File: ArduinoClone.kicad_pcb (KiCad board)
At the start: 2 copper layers, 0 parts

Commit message: added design rules
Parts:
- added BT1: Battery 3V, Connector_PinHeader_2.54mm:PinHeader_1x02_P2.54mm_Vertical, F.Cu at (177.0, 88.4)
- added C1: 22pF, Capacitor_SMD:C_0805_2012Metric_Pad1.15x1.40mm_HandSolder, F.Cu at (181.7, 87.6)
- added C2: 22pF, Capacitor_SMD:C_0805_2012Metric_Pad1.15x1.40mm_HandSolder, F.Cu at (177.0, 94.8)
- added C3: 10uF, Capacitor_SMD:C_0805_2012Metric_Pad1.15x1.40mm_HandSolder, F.Cu at (181.7, 90.5)
- added D1: LED, LED_SMD:LED_0805_2012Metric_Pad1.15x1.40mm_HandSolder, F.Cu at (170.8, 96.7)
- added J1: Serial, Connector_PinSocket_2.54mm:PinSocket_1x04_P2.54mm_Vertical, F.Cu at (94.4, 77.2)
- added J2: Digital pins, Connector_PinSocket_2.54mm:PinSocket_1x09_P2.54mm_Vertical, F.Cu at (89.8, 77.2)
- added J3: I2C, Connector_PinSocket_2.54mm:PinSocket_1x04_P2.54mm_Vertical, F.Cu at (99.0, 77.2)
- added J4: ICSP, Connector_PinSocket_2.54mm:PinSocket_2x03_P2.54mm_Vertical, F.Cu at (106.2, 77.2)
- added R1: 330R, Resistor_SMD:R_0805_2012Metric_Pad1.15x1.40mm_HandSolder, F.Cu at (175.6, 97.7)
- added R2: 10K, Resistor_SMD:R_0805_2012Metric_Pad1.15x1.40mm_HandSolder, F.Cu at (181.8, 93.5)
- added U1: DS1337S+, Package_SO:SO-8_5.3x6.2mm_P1.27mm, F.Cu at (158.0, 96.6)
- added U2: 24LC1025, Package_SO:SOIJ-8_5.3x5.3mm_P1.27mm, F.Cu at (169.4, 84.7)
- added U3: 24LC1025, Package_SO:SOIJ-8_5.3x5.3mm_P1.27mm, F.Cu at (169.4, 91.7)
- added U4: ATMEGA328-AU, digikey-footprints:TQFP-32_7x7mm, F.Cu at (158.4, 87.0)
- added Y1: Crystal 32MHz, Crystal:Crystal_SMD_MicroCrystal_CC7V-T1A-2Pin_3.2x1.5mm, F.Cu at (165.9, 96.9)
- added Y2: Crystal 16MHz, Crystal:Crystal_SMD_5032-2Pin_5.0x3.2mm_HandSoldering, F.Cu at (179.8, 83.7)
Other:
- net class Power added: clearance 0.2, trace_width 0.3, via_dia 1, via_drill 0.6

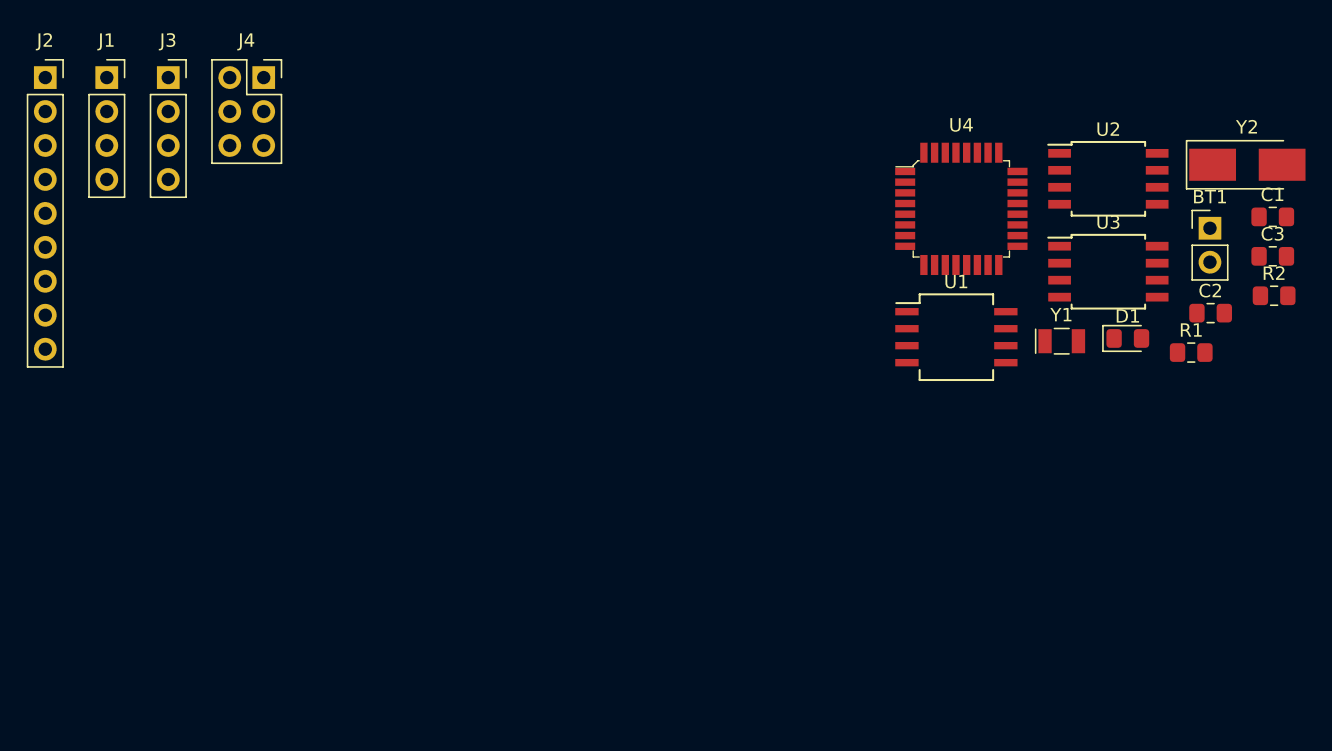
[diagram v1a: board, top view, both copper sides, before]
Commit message: corrected error inschematic and placed components in pcbnew
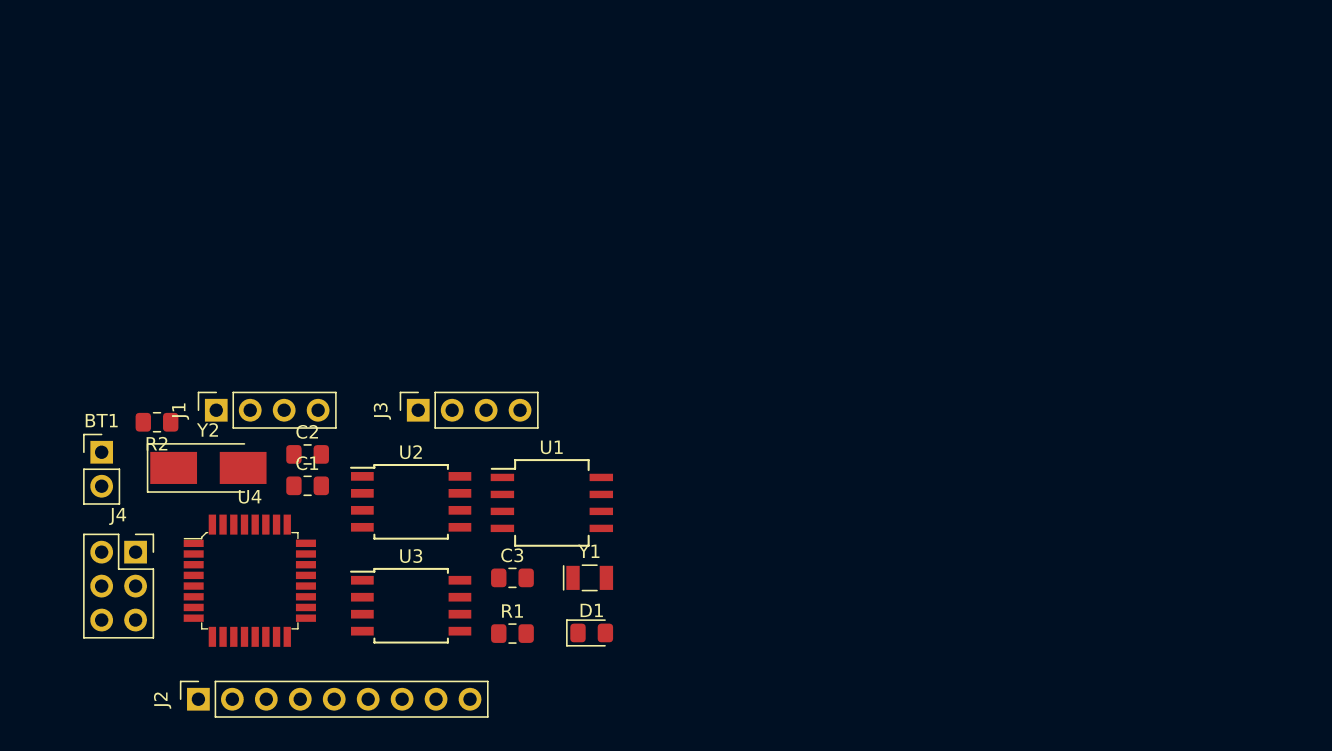
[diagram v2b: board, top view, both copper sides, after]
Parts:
- moved BT1 84.6 mm to (94.1, 105.2)
- moved R2 84.1 mm to (98.2, 102.9), turned to 180 degrees
- moved Y2 81.0 mm to (102.0, 106.4)
- moved C1 75.0 mm to (109.5, 107.7)
- moved C2 68.4 mm to (109.5, 105.3)
- moved C3 61.8 mm to (124.8, 114.6)
- moved U4 60.1 mm to (105.1, 114.8)
- moved U3 57.8 mm to (117.2, 116.7)
- moved U2 57.5 mm to (117.2, 108.9)
- moved R1 55.0 mm to (124.8, 118.7)
- moved J2 47.9 mm to (101.3, 123.7), turned to 90 degrees
- moved D1 45.8 mm to (130.7, 118.7)
- moved Y1 39.5 mm to (130.6, 114.6)
- moved J4 36.8 mm to (96.6, 112.7)
- moved U1 32.7 mm to (127.7, 109.0)
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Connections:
- BT1 pad 2: Net-(BT1-Pad2) -> GNDPWR
- C3 pad 1: Net-(BT1-Pad2) -> /Vcc

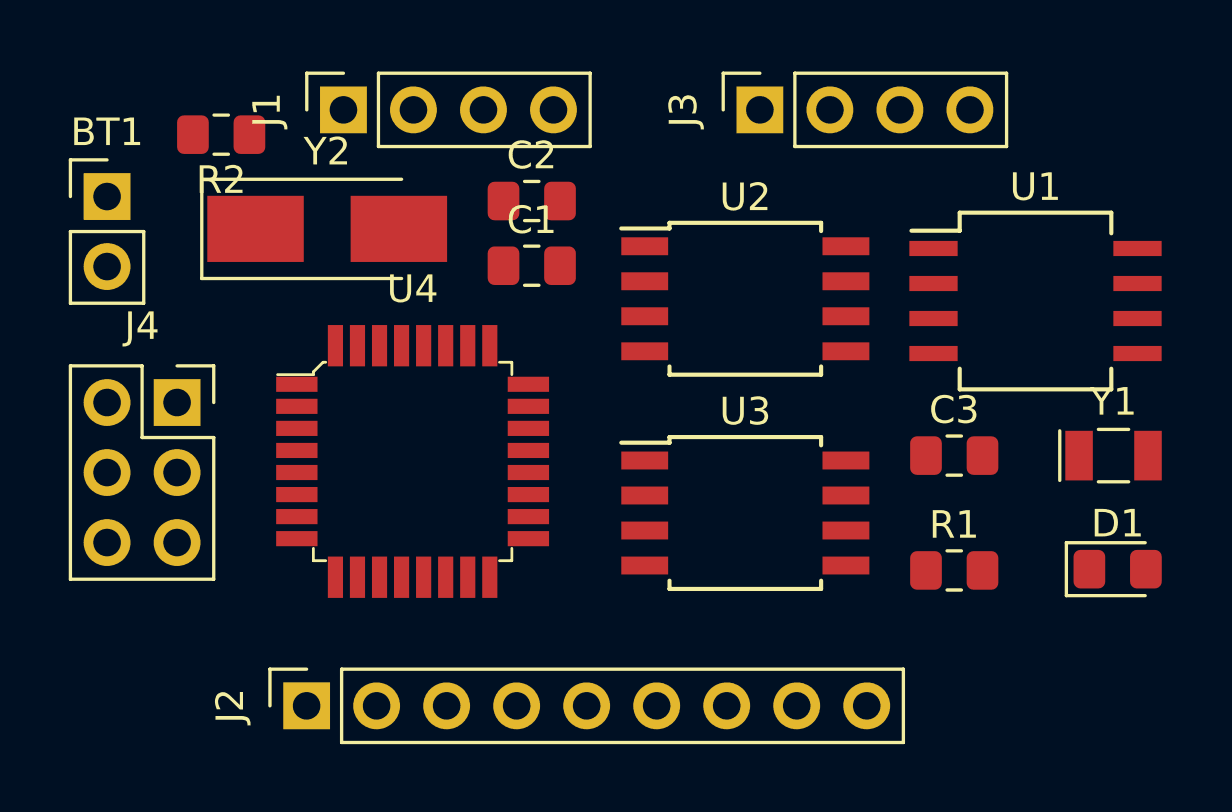
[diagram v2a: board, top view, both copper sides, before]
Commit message: added edges to board
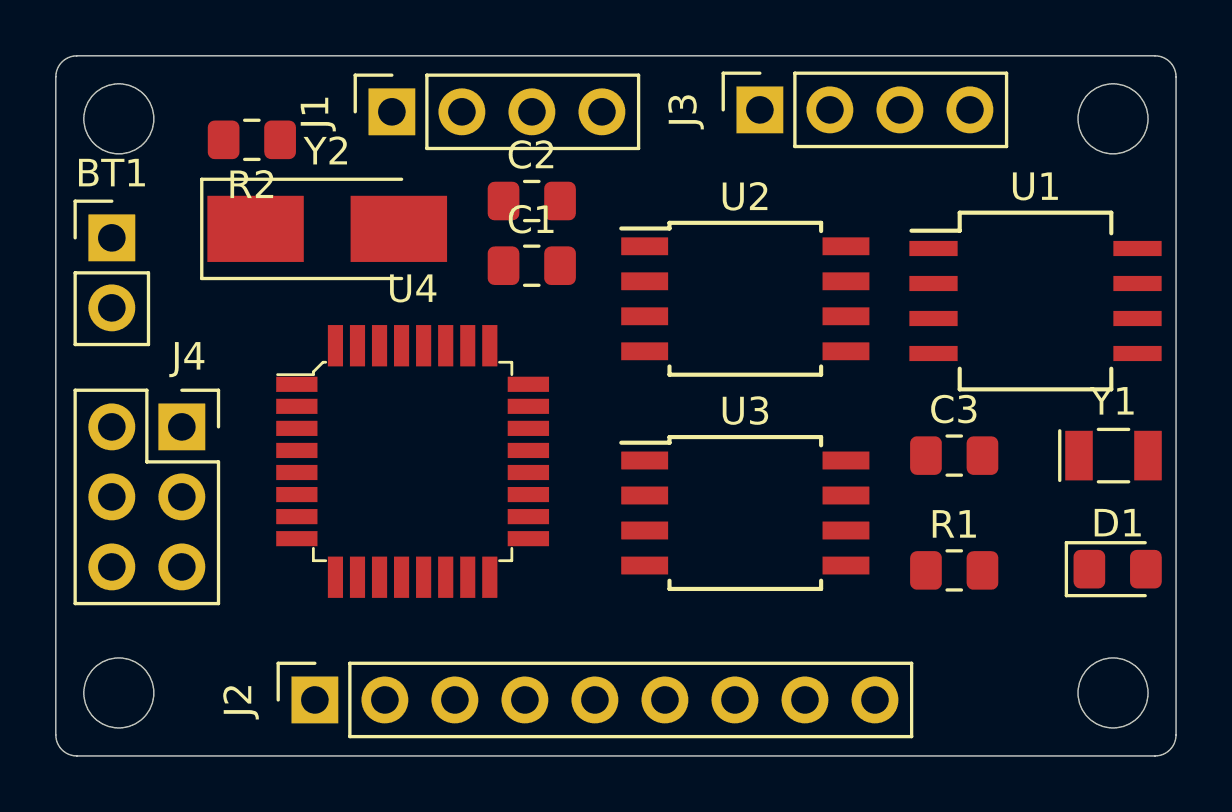
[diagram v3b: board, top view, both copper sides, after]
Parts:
- moved J1 1.76 mm to (104.4, 102.1)
- moved BT1 1.51 mm to (94.2, 106.7)
- moved R2 1.13 mm to (99.3, 103.1)
- moved J4 0.90 mm to (96.8, 113.5)
- moved J2 0.37 mm to (101.6, 123.4)
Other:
- board outline added: 40.6 x 25.4 mm
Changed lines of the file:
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@@
   (general
     (thickness 1.6)
-    (drawings 0)
+    (drawings 12)
     (tracks 0)
     (zones 0)
@@
   )
   (module Connector_PinHeader_2.54mm:PinHeader_1x02_P2.54mm_Vertical (layer F.Cu)
-    (at 94.06128 105.1814)
+    (at 94.234 106.68)
     (descr "Through hole straight pin header, 1x02, 2.54mm pitch, single row")
     (tags "Through hole pin header THT 1x02 2.54mm single row")
@@
   )
   (module Connector_PinSocket_2.54mm:PinSocket_1x04_P2.54mm_Vertical (layer F.Cu)
-    (at 102.63632 102.03688 90)
+    (at 104.394 102.108 90)
     (descr "Through hole straight socket strip, 1x04, 2.54mm pitch, single row (from Kicad 4.0.7), script generated")
     (tags "Through hole socket strip THT 1x04 2.54mm single row")
@@
   )
   (module Connector_PinSocket_2.54mm:PinSocket_1x09_P2.54mm_Vertical (layer F.Cu)
-    (at 101.30028 123.65736 90)
+    (at 101.6 123.444 90)
     (descr "Through hole straight socket strip, 1x09, 2.54mm pitch, single row (from Kicad 4.0.7), script generated")
     (tags "Through hole socket strip THT 1x09 2.54mm single row")
@@
   )
   (module Connector_PinSocket_2.54mm:PinSocket_2x03_P2.54mm_Vertical (layer F.Cu)
-    (at 96.60128 112.65408)
+    (at 96.774 113.538)
     (descr "Through hole straight socket strip, 2x03, 2.54mm pitch, double cols (from Kicad 4.0.7), script generated")
     (tags "Through hole socket strip THT 2x03 2.54mm double row")
-    (fp_text reference J4 (at -1.27 -2.77) (layer F.SilkS)
+    (fp_text reference J4 (at 0.254 -2.54) (layer F.SilkS)
       (effects (font (size 1 1) (thickness 0.15)))
     )
@@
   )
   (module Resistor_SMD:R_0805_2012Metric_Pad1.15x1.40mm_HandSolder (layer F.Cu)
-    (at 98.20148 102.93604 180)
+    (at 99.314 103.124 180)
     (descr "Resistor SMD 0805 (2012 Metric), square (rectangular) end terminal, IPC_7351 nominal with elongated pad for handsoldering. (Body size source: https://docs.google.com/spreadsheets/d/1BsfQQcO9C6DZCsRaXUlFlo91Tg2WpOkGARC1WS5S8t0/edit?usp=sharing), generated with kicad-footprint-generator")
     (tags "resistor handsolder")
@@
     )
   )
+  (gr_circle (center 130.556 102.362) (end 129.54 101.6) (layer Edge.Cuts) (width 0.05))
+  (gr_circle (center 130.556 123.19) (end 129.54 122.428) (layer Edge.Cuts) (width 0.05))
+  (gr_circle (center 94.488 123.19) (end 93.472 122.428) (layer Edge.Cuts) (width 0.05))
+  (gr_circle (center 94.488 102.362) (end 93.472 101.6) (layer Edge.Cuts) (width 0.05))
+  (gr_arc (start 132.08 124.714) (end 132.08 125.476) (angle -90) (layer Edge.Cuts) (width 0.05))
+  (gr_arc (start 92.964 124.714) (end 92.202 124.714) (angle -90) (layer Edge.Cuts) (width 0.05))
+  (gr_arc (start 92.964 100.838) (end 92.964 100.076) (angle -90) (layer Edge.Cuts) (width 0.05))
+  (gr_arc (start 132.08 100.838) (end 132.842 100.838) (angle -90) (layer Edge.Cuts) (width 0.05))
+  (gr_line (start 132.842 124.714) (end 132.842 100.838) (layer Edge.Cuts) (width 0.05))
+  (gr_line (start 92.964 125.476) (end 132.08 125.476) (layer Edge.Cuts) (width 0.05))
+  (gr_line (start 92.202 100.838) (end 92.202 124.714) (layer Edge.Cuts) (width 0.05))
+  (gr_line (start 132.08 100.076) (end 92.964 100.076) (layer Edge.Cuts) (width 0.05))
 )

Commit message: routed
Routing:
- net GNDPWR: track 0.00 -> 118.2 mm, vias 0 -> 9
- net /Vcc: track 0.00 -> 103.0 mm
- net /SCK: track 0.00 -> 63.5 mm, vias 0 -> 7
- net /SDA: track 0.00 -> 53.0 mm, vias 0 -> 6
- net /MISO: track 0.00 -> 38.5 mm, vias 0 -> 2
- net /RESET: track 0.00 -> 34.9 mm, vias 0 -> 2
- net Net-(D1-Pad2): track 0.00 -> 29.0 mm
- net Net-(C1-Pad1): track 0.00 -> 28.6 mm, vias 0 -> 4
- net /MOSI: track 0.00 -> 26.6 mm, vias 0 -> 2
- net /ADDS1: track 0.00 -> 22.9 mm, vias 0 -> 2
- net Net-(C2-Pad1): track 0.00 -> 22.3 mm, vias 0 -> 2
- net /D4: track 0.00 -> 22.3 mm, vias 0 -> 2
- net /D2: track 0.00 -> 17.7 mm, vias 0 -> 1
- net /D3: track 0.00 -> 17.5 mm, vias 0 -> 1
- net /Tx: track 0.00 -> 16.4 mm, vias 0 -> 2
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
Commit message: completed Arduino
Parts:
- added G***: LOGO, my_library:simonpiazolo_logo_6mm, B.Cu at (117.3, 118.6)
- added REF**: OSHW-Logo2_7.3x6mm_SilkScreen, Symbol:OSHW-Logo2_7.3x6mm_SilkScreen, B.Cu at (99.1, 109.0)
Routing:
- net /MISO: track 38.5 -> 25.7 mm
- net /MOSI: track 26.6 -> 17.8 mm, vias 2 -> 3
- net GNDPWR: track 118.2 -> 122.5 mm
- net /D2: track 17.7 -> 18.4 mm
- net /D3: track 17.5 -> 18.1 mm
- added copper zone on B.Cu, net GNDPWR
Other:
- board text added: "Arduino Clone -2Mbit EEPROM -clock & calendar -I2C, SPI, GPIO"
- board text added: "D2"
- board text added: "D3"
- board text added: "D4"
- board text added: "D5"
- board text added: "D6"
- board text added: "D7"
- board text added: "D8"
- board text added: "GND"
- board text added: "MISO"
- board text added: "REST"
- board text added: "Rx"
- board text added: "SCK"
- board text added: "SDA"
- board text added: "Tx"
- board text added: "Vcc"
